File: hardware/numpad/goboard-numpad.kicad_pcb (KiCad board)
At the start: 2 copper layers, 74.9 x 104.1 mm, 51 parts, among them J1 Conn_02x05_Odd_Even, J2 Conn_01x01, J3 Conn_01x05, J4 Conn_01x02_Female, J5 Conn_01x02_Male, SW1 SW_Push, SW10 5, SW12 2, SW13 dot, SW14 times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

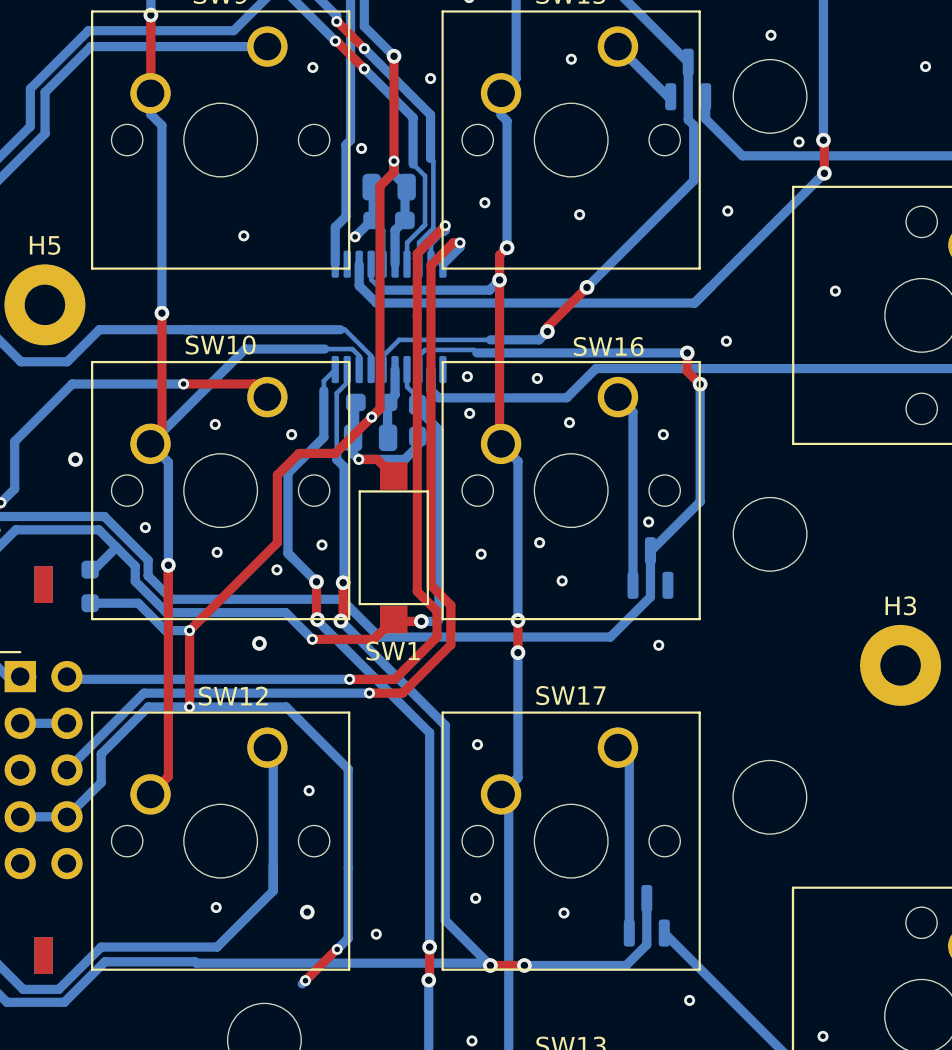
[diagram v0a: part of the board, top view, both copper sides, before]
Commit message: Numpad: Re-route traces to improve ground plane
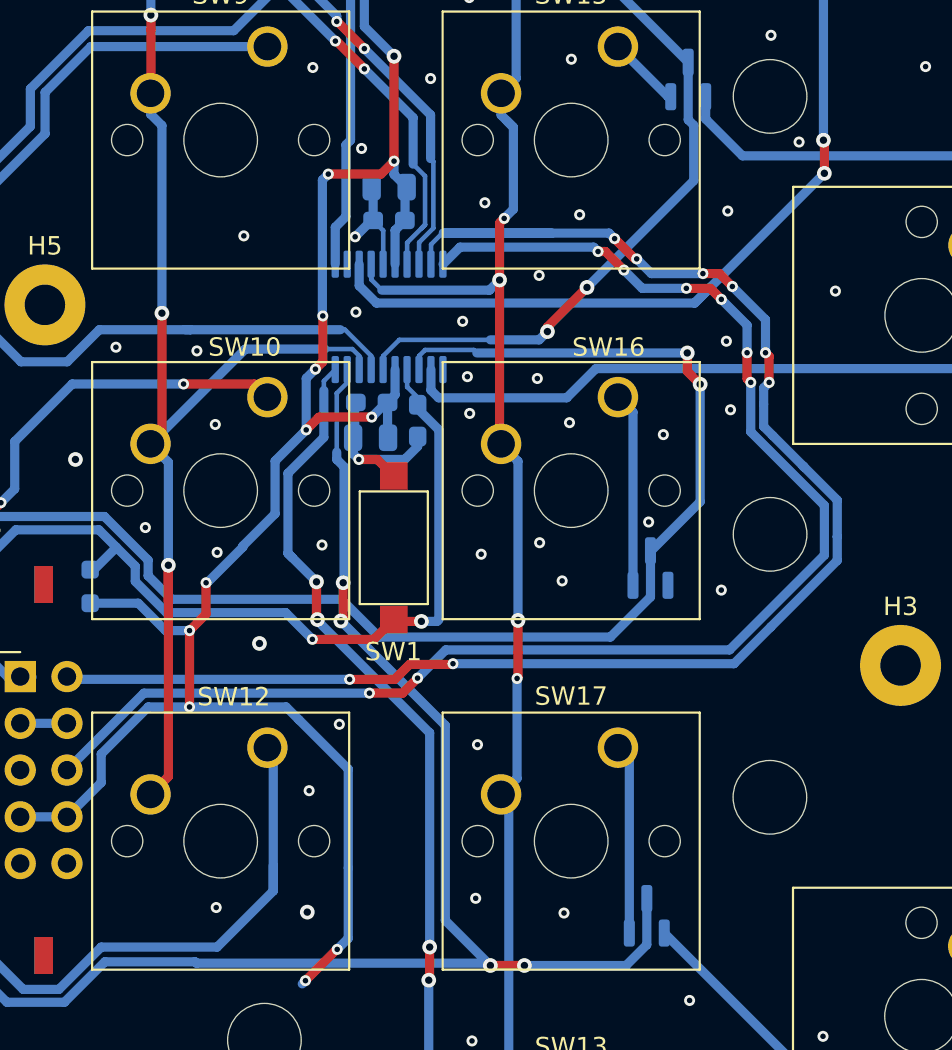
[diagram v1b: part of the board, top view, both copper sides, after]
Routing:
- net /SWDIO: track 46.8 -> 86.9 mm, vias 2 -> 8
- net /SWDCLK: track 48.4 -> 79.0 mm, vias 2 -> 8
- net VCC: track 207.2 -> 211.6 mm, vias 10 -> 15
- net GND: vias 86 -> 90

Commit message: Main & Numpad: Add release info to PCBs
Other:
- board text added: "License: CERN Open Hardware License v1."
- board text added: "https://github.com/ BerndGottschlag/goboard V1.0"
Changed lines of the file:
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@@
     (property "Sheetname" "Keys")
     (attr through_hole)
-    (fp_text reference "SW13" (at -2.54 -2.794) (layer "F.SilkS")
+    (fp_text reference "SW13" (at -2.54 12.8875) (layer "F.SilkS")
       (effects (font (size 1 1) (thickness 0.15)))
     )
@@
   (gr_line (start 180.6 147.5) (end 180.6 63.4) (layer "Edge.Cuts") (width 0.1))
   (gr_arc (start 175.6 147.5) (end 175.6 152.5) (angle -90) (layer "Edge.Cuts") (width 0.1))
+  (gr_text "https://github.com/\nBerndGottschlag/goboard\nV1.0" (at 152.7 133.8) (layer "F.SilkS")
+    (effects (font (size 1 1) (thickness 0.15)))
+  )
+  (gr_text "License: CERN Open\nHardware License v1." (at 170.8 76.9) (layer "F.SilkS")
+    (effects (font (size 1 1) (thickness 0.15)))
+  )
   (segment (start 131.55 96.35) (end 131.25 96.35) (width 0.5) (layer "B.Cu") (net 1))
   (segment (start 120.59875 96.35) (end 122.34125 98.0925) (width 0.5) (layer "B.Cu") (net 1))
